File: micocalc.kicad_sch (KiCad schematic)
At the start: 41 parts, among them J1 Conn_01x02, J2 Conn_01x04, SW1 SW_Push_45deg, SW10 SW_Push_45deg, SW11 SW_Push_45deg, SW12 SW_Push_45deg, SW13 SW_Push_45deg, SW14 SW_Push_45deg, SW15 SW_Push_45deg, SW16 SW_Push_45deg, SW17 SW_SPST, SW18 SW_Push, SW2 SW_Push_45deg, SW3 SW_Push_45deg, SW4 SW_Push_45deg, SW5 SW_Push_45deg, SW6 SW_Push_45deg, SW7 SW_Push_45deg, SW8 SW_Push_45deg, SW9 SW_Push_45deg, U1 STM32L431RCTx, U2 HS96L03W2C03, U3 MCP1700x-120xxTT, Y1 8MHz

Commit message: improvements, better buttons
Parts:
- added C12, C13, C14, C15, C16, C17, C18, C19, C20, C21, C22, C23, C24, C25, C26, C27: 1u, Capacitor_SMD:C_0603_1608Metric_Pad1.08x0.95mm_HandSolder, symbol Device:C_Small
- added R10, R11, R12, R13, R14, R15, R16, R17, R18, R3, R4, R5, R6, R7, R8, R9: 2.2k, Resistor_SMD:R_0603_1608Metric_Pad0.98x0.95mm_HandSolder, symbol Device:R_Small_US
- C10, C11: footprint Capacitor_THT:C_Disc_D3.0mm_W2.0mm_P2.50mm -> Capacitor_SMD:C_0603_1608Metric_Pad1.08x0.95mm_HandSolder
- C3, C4, C5, C6, C7, C8, C9: value 0.1u -> 1u
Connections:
- net GND: now also C12.2, C13.2, C14.2, C15.2, C16.2, C17.2, C18.2, C19.2, C20.2, C21.2, C22.2, C23.2, C24.2, C25.2, C26.2, C27.2
- net at SW8.1: now also R10.2; no longer U1.20 (PA4)
- net at SW9.1: now also R11.2; no longer U1.44 (PA11)
- net at SW4.1: now also R6.2; no longer U1.14 (PA0)
- net at SW15.1: now also R17.2; no longer U1.56 (PB4)
- net at U1.55 (PB3): now also C27.1, R18.1; no longer SW16.1
- net at SW14.1: now also R16.2; no longer U1.57 (PB5)
- net at U1.15 (PA1): now also C14.1, R5.1; no longer SW3.1
- net at U1.21 (PA5): now also C18.1, R9.1; no longer SW7.1
- net at U1.43 (PA10): now also C21.1, R12.1; no longer SW10.1
- net at U1.17 (PA3): now also C12.1, R3.1; no longer SW1.1
- net at U1.58 (PB6): now also C24.1, R15.1; no longer SW13.1
- net at U1.41 (PA8): now also C23.1, R14.1; no longer SW12.1
- net at U1.22 (PA6): now also C17.1, R8.1; no longer SW6.1
- net at U1.23 (PA7): now also C16.1, R7.1; no longer SW5.1
- net at U1.16 (PA2): now also C13.1, R4.1; no longer SW2.1
- net at SW11.1: now also R13.2; no longer U1.42 (PA9)
- new net: R8.2, SW6.1
- new net: R14.2, SW12.1
- new net: R18.2, SW16.1
- new net: R12.2, SW10.1
- new net: R3.2, SW1.1
- new net: R5.2, SW3.1
- new net: C19.1, R10.1, U1.20 (PA4)
- new net: C26.1, R17.1, U1.56 (PB4)
- new net: R7.2, SW5.1
- new net: C22.1, R13.1, U1.42 (PA9)
- new net: C15.1, R6.1, U1.14 (PA0)
- new net: C25.1, R16.1, U1.57 (PB5)
- new net: R15.2, SW13.1
- new net: R9.2, SW7.1
- new net: C20.1, R11.1, U1.44 (PA11)
- new net: R4.2, SW2.1
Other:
- moved on the sheet: SW1, SW2, SW3, SW4

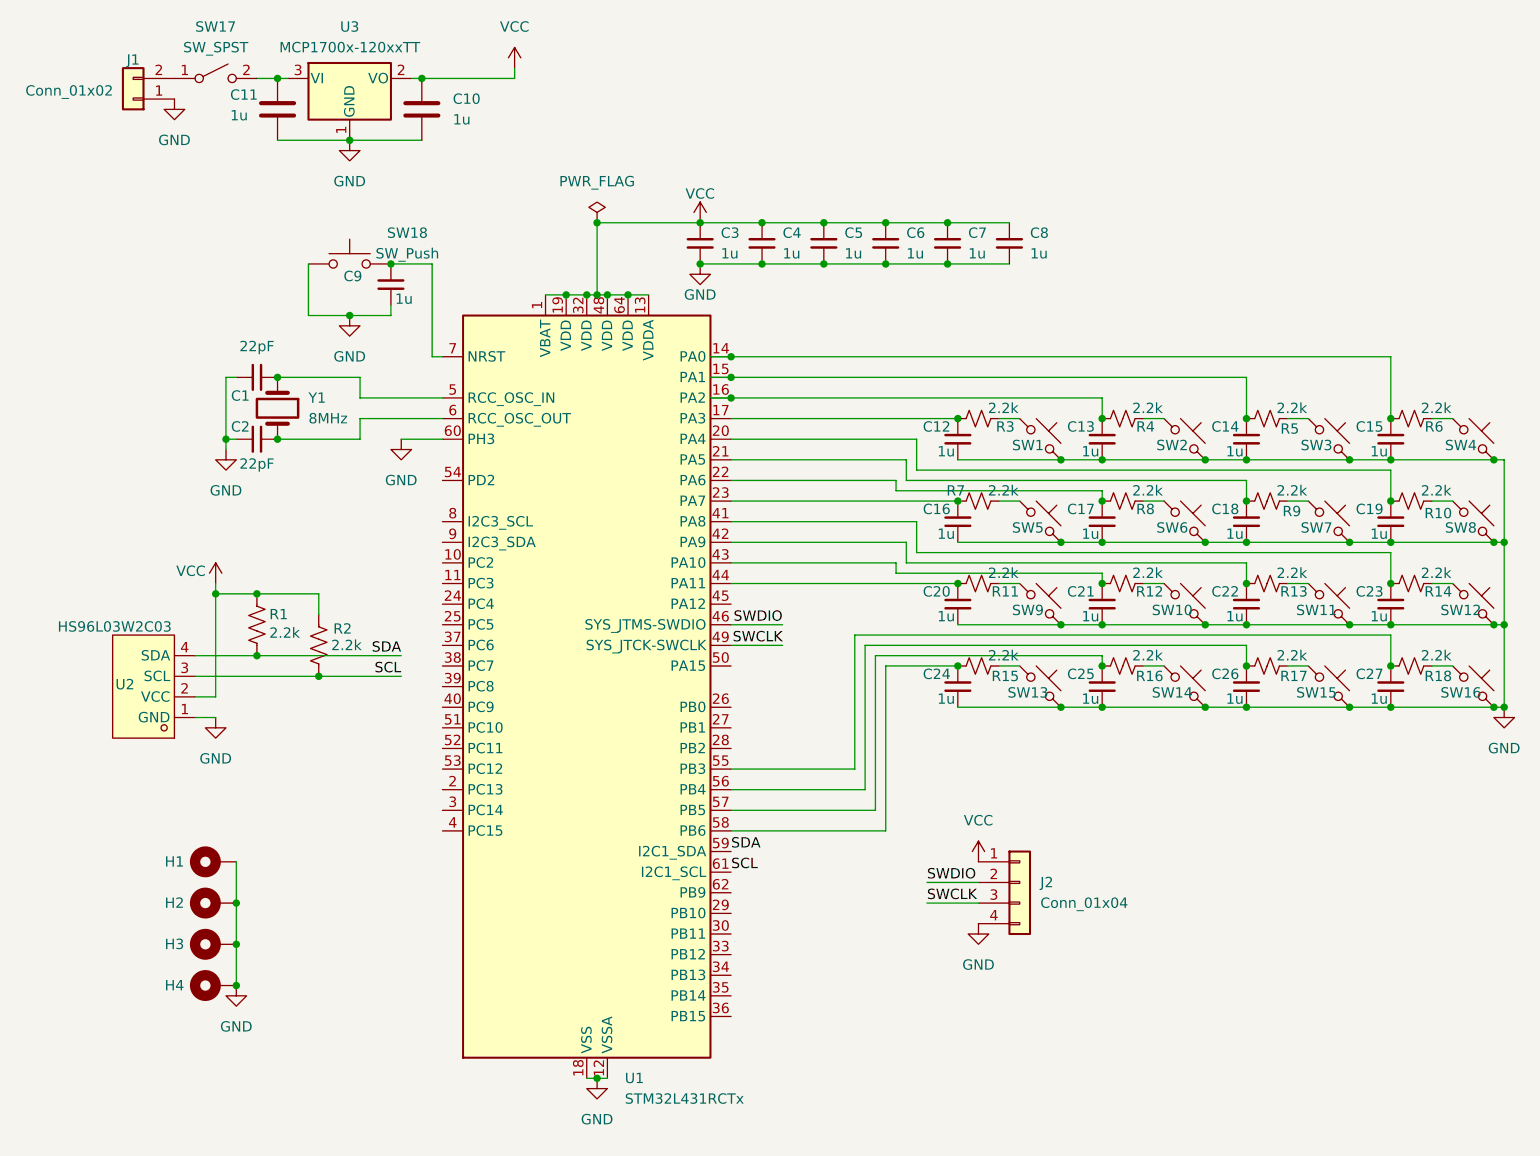
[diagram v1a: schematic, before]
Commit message: route SWO out
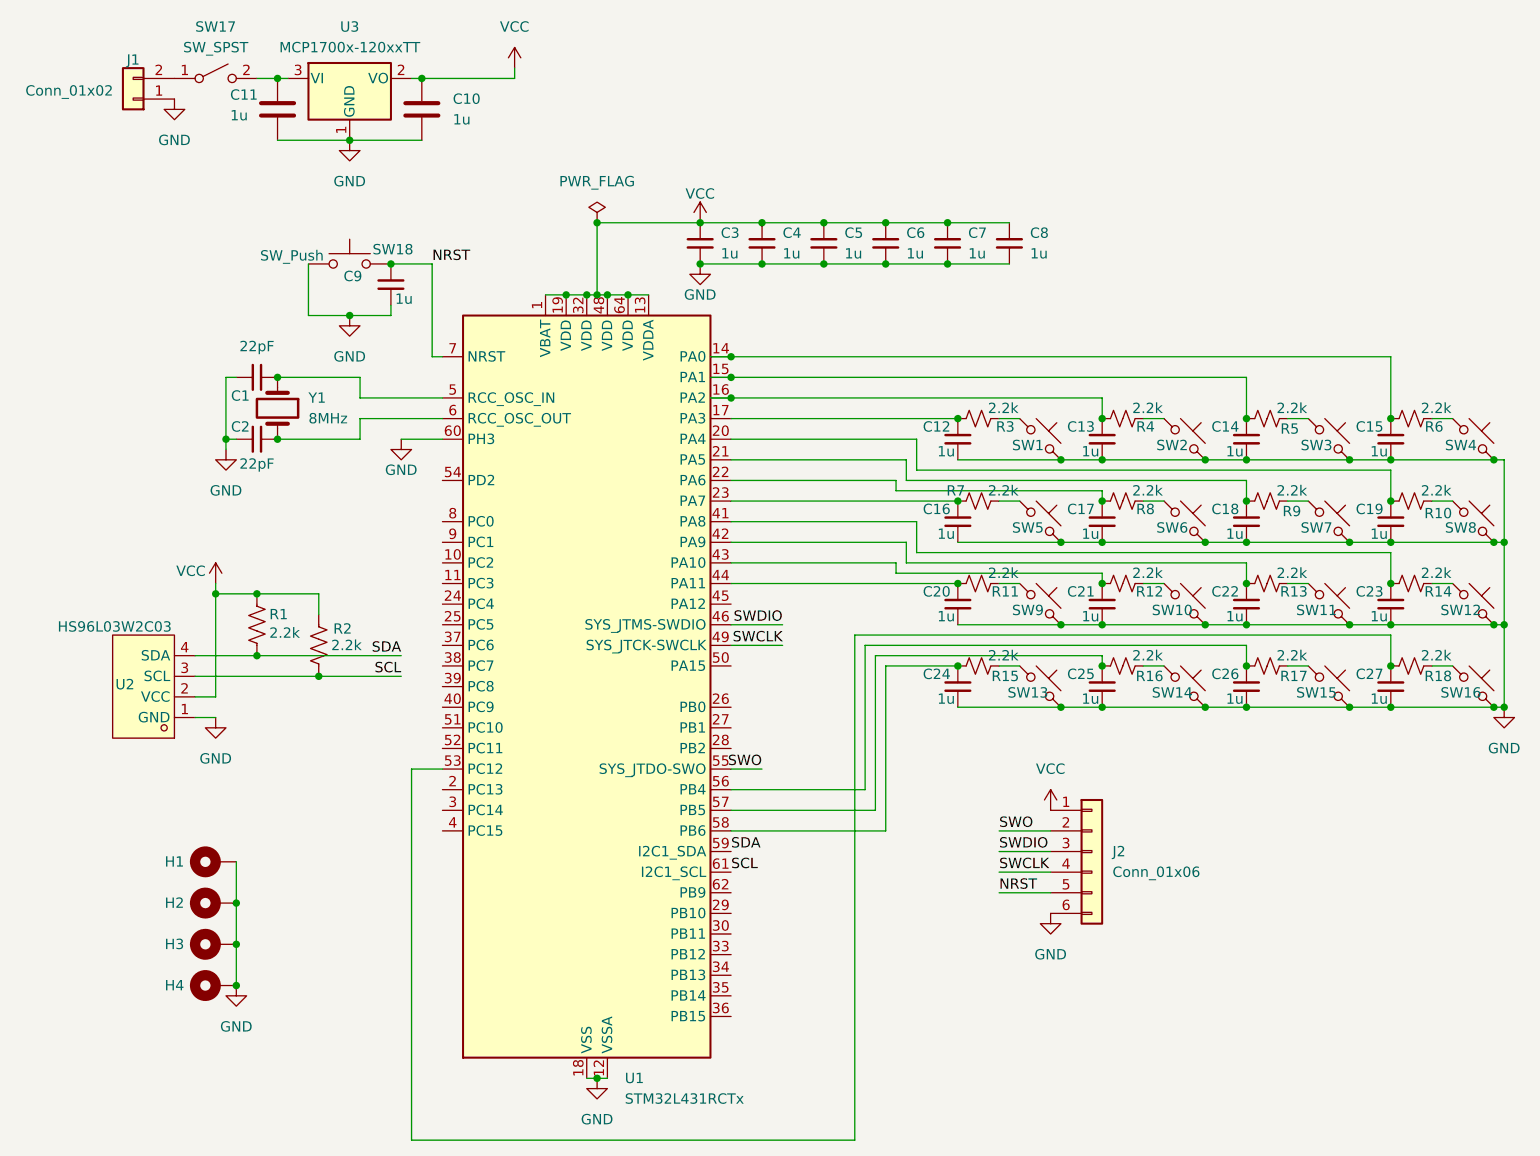
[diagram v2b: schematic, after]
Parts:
- removed J2: Conn_01x04, Connector_PinHeader_2.54mm:PinHeader_1x04_P2.54mm_Horizontal, symbol Connector_Generic:Conn_01x04
- added J2: Conn_01x06, Connector_PinSocket_2.54mm:PinSocket_1x06_P2.54mm_Vertical, symbol Connector_Generic:Conn_01x06
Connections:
- net GND: now also J2.6 (Pin_6)
- net SWCLK: now also J2.4 (Pin_4)
- net SWDIO: now also J2.3 (Pin_3)
- net VCC: now also J2.1 (Pin_1)
- net at C27.1, R18.1: now also U1.53 (PC12); no longer U1.55 (PB3)
- net NRST: now reaches C9.1, SW18.2, U1.7 (NRST)
- net NRST: now also J2.5 (Pin_5)
- new net SWO: J2.2 (Pin_2), U1.55 (PB3)
